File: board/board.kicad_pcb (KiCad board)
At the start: 2 copper layers, 21 x 13 mm, 16 parts, among them J1 013_PoE_rectified, J2 014_PoE_controlled, Q1 PSMN5R2-60YL, U1 LT4275AIDDPBF-LT4275AIDDPBF

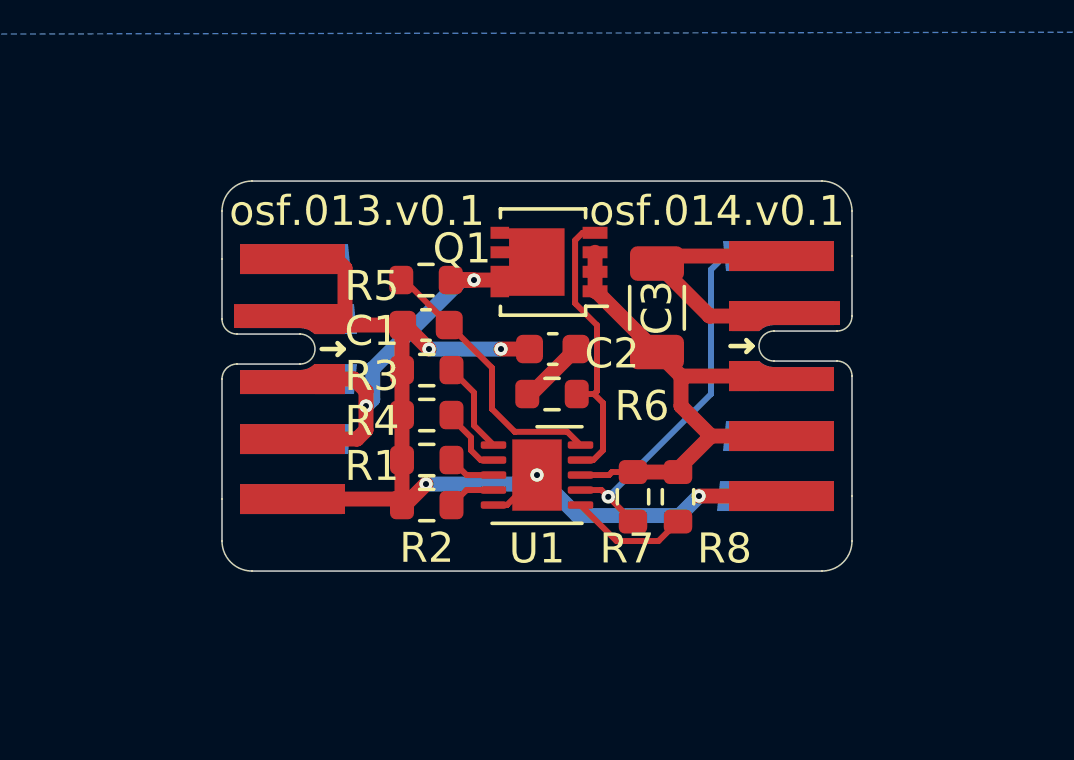
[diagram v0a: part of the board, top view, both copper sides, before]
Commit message: changed fp Q1 to back
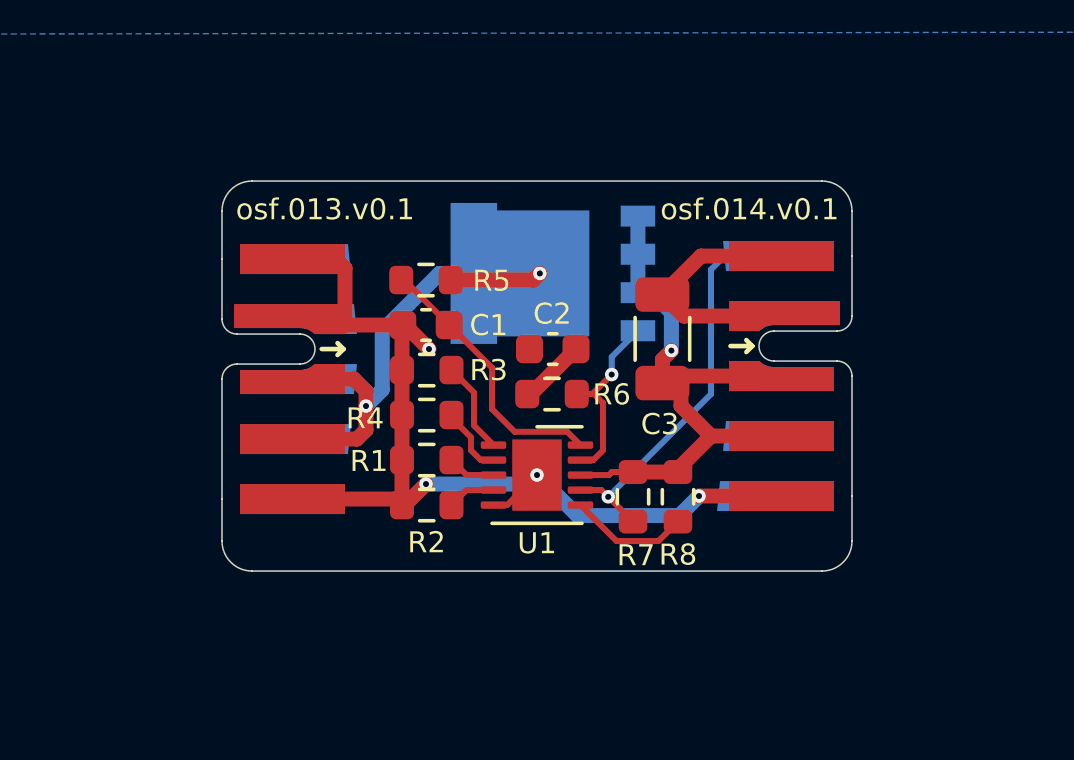
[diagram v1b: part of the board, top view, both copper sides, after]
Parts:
- removed LOGO1: Logo_Open_Hardware_Small, Symbol:OSHW-Logo2_9.8x8mm_SilkScreen
- Q1: footprint Package_TO_SOT_SMD:LFPAK33 -> Package_TO_SOT_SMD:LFPAK56; moved to B.Cu
- moved C3 1.05 mm to (91.7, 79.3)
- moved Q1 0.40 mm to (88.0, 77.1)
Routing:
- net GND: track 44.2 -> 40.5 mm, vias 5 -> 4
- net Net-(Q1-Pad4): track 9.70 -> 6.72 mm, vias 0 -> 1
- net /Controller/poe+_in: track 15.1 -> 17.1 mm
- net /Controller/poe+_out: track 17.1 -> 18.9 mm, vias 0 -> 1
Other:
- board text added: "osf.b027.v0.2"
- board text removed: "osf.b027.v0.1"
